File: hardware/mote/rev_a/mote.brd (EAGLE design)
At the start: 160 x 100 mm, 37 parts, among them Q1 CSD22206W, Q2 CSD75207W15, Q3 CSD75207W15, Q4 CSD13303W1015, Q5 CSD22206W, U1 NRF52840, U3 MAX17222, U4 TPS3839G25DBZ, X1 7V-32.000MAHV-T

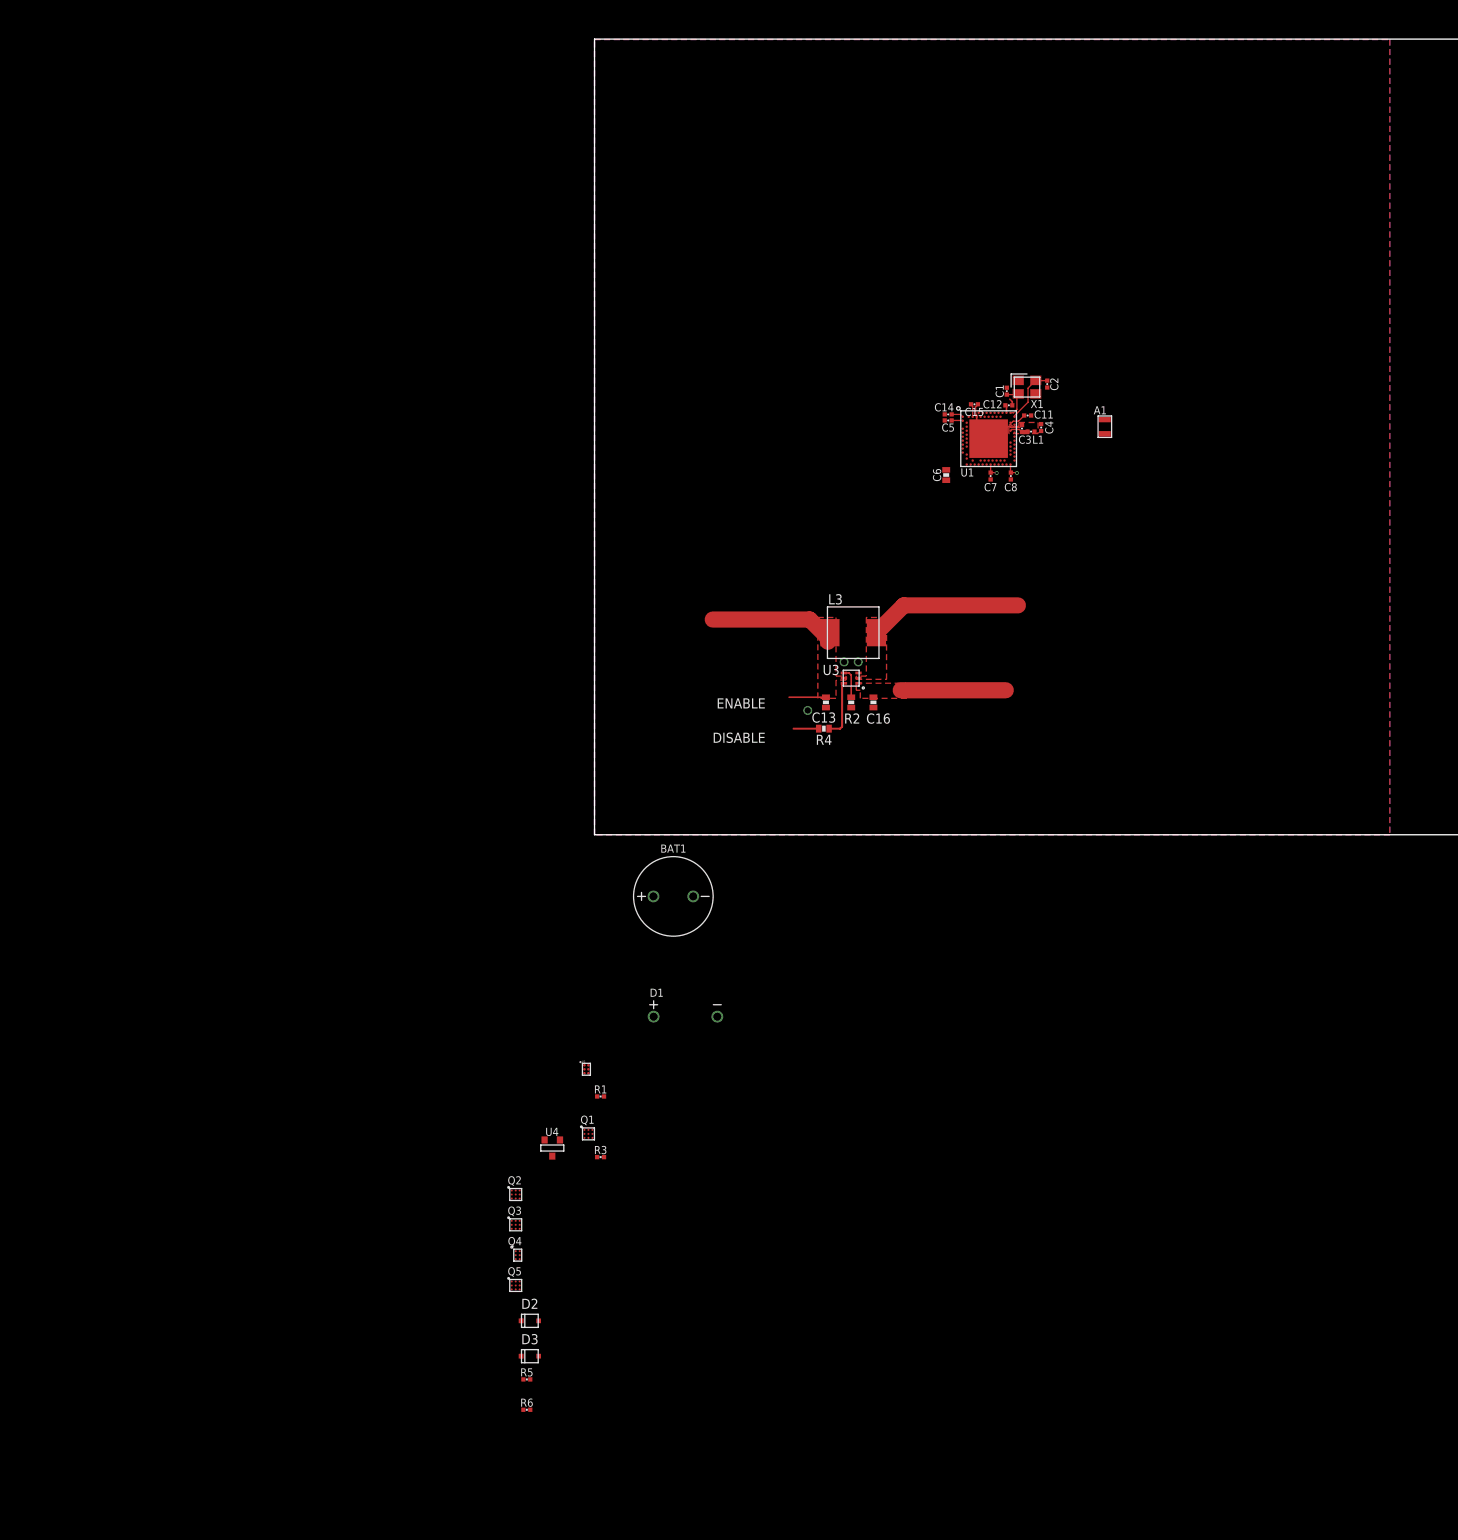
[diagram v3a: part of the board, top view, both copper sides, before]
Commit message: finish power supply, rtc
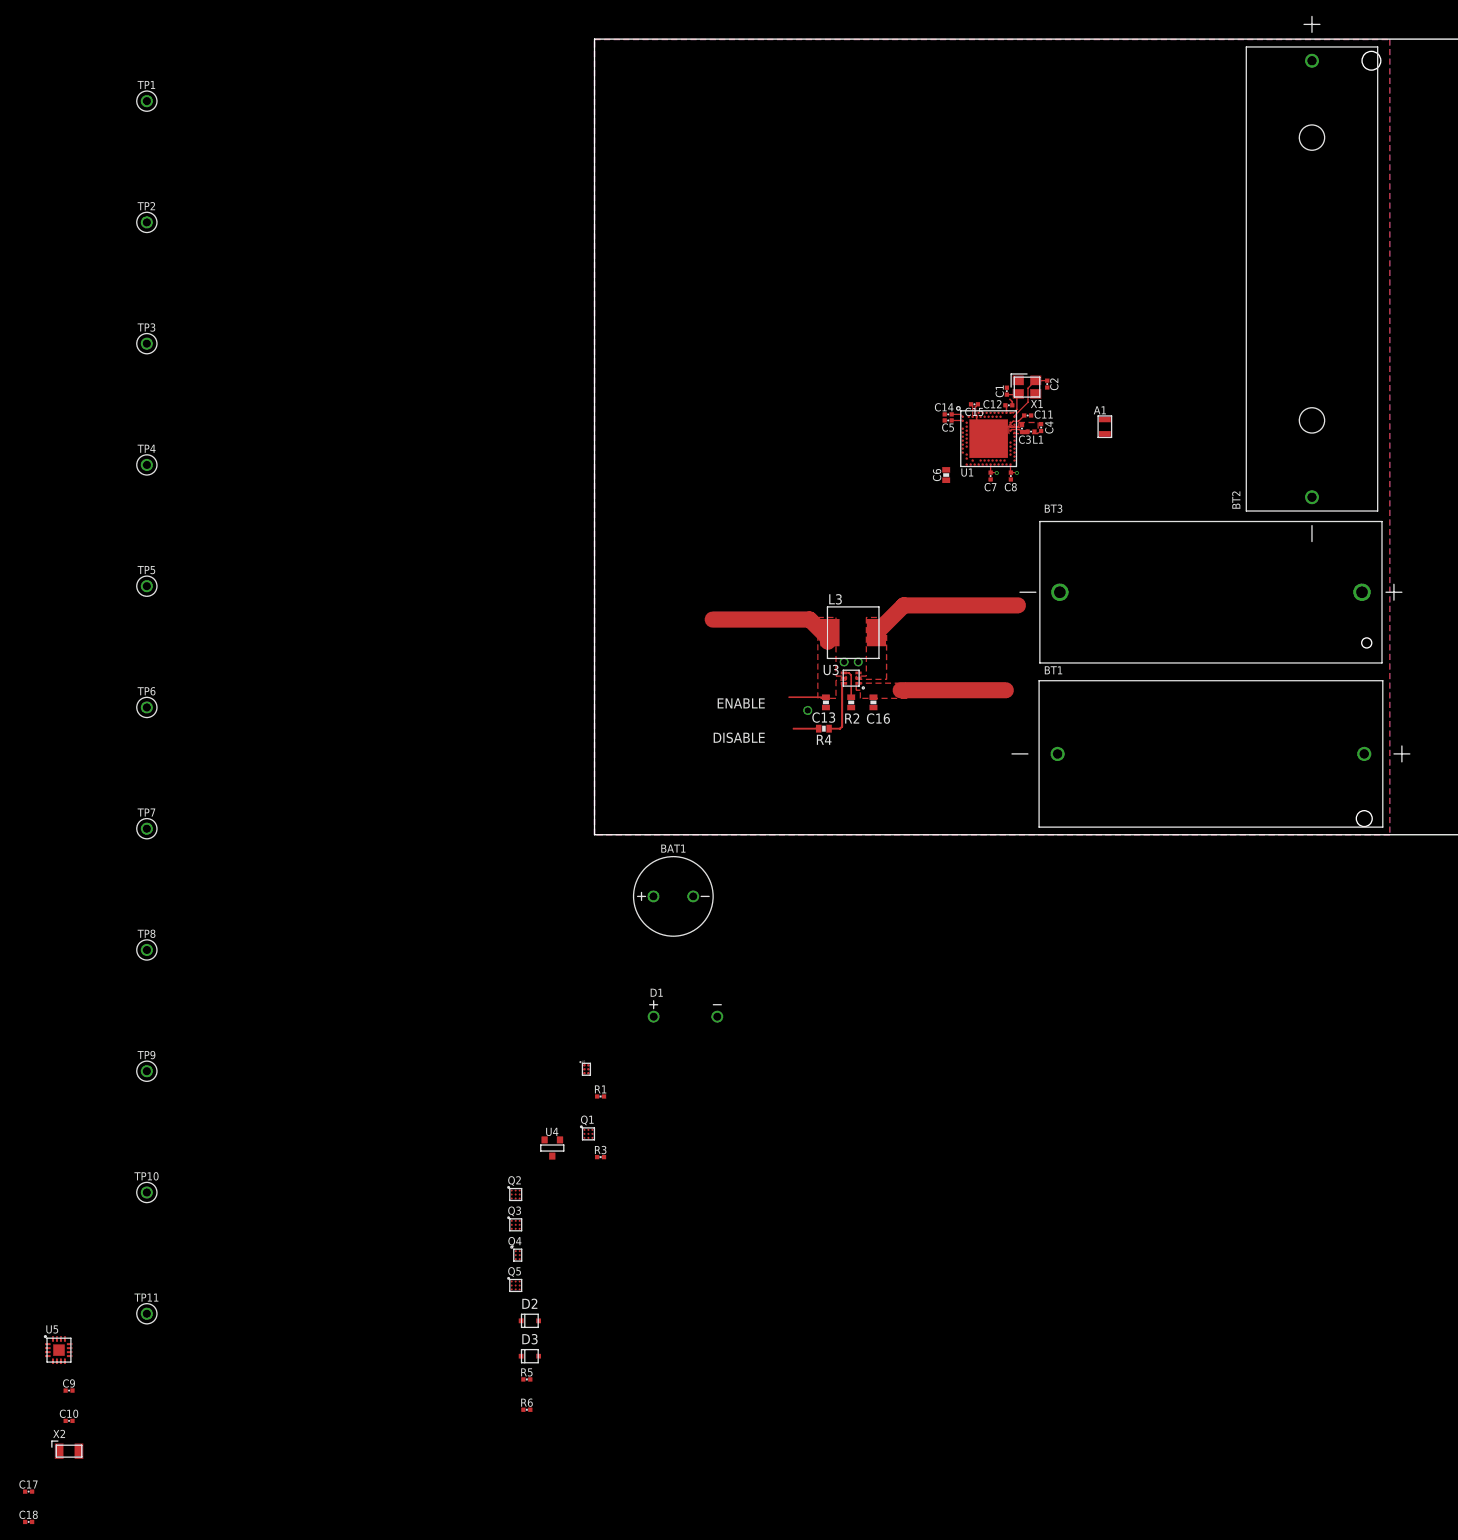
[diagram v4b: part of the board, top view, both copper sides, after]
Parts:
- added BT1: BAT_PACK2/3AA, batteries:6S-2-3A
- added BT2: BAT_PACKAA, batteries:BHAA-3
- added BT3: BAT_PACKCR123A, batteries:BH123A
- added C10: 1uF, passives:0402_CAP
- added C17, C18: DNP, passives:0402_CAP
- added C9: 47pF, passives:0402_CAP
- added TP1, TP10, TP11, TP2, TP3, TP4, TP5, TP6, TP7, TP8, TP9: TEST_POINT_0.040IN, headers:TESTPOINT_0.040IN
- added U5: AB1815-T3, chips:QFN-16-3MM
- added X2: ABS07-32.768KHZ-7-T, crystals:2-SMD
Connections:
- new net !RTC_EXTR: U5.3
- new net !RTC_IRQ1: U5.11
- new net !RTC_IRQ2: U5.4
- new net !RTC_RESET: U5.1
- new net CLKOUT: U1.D2, U5.8
- new net CS_RTC: U5.12
- new net MISO: U5.6
- new net MOSI: U5.9
- new net N$18: D3.P$1, Q3.A1, Q3.C1, R6.2, TP6.TESTPOINT
- new net N$19: C17.1, U5.16, X2.1
- new net N$20: C18.1, U5.15, X2.2
- new net N$21: C9.1, U5.14
- new net N$22: BT1.+, BT2.+, BT3.+, Q3.A2, Q3.A3, Q3.B3, TP9.TESTPOINT
- new net N$24: BAT1.+, D1.+, Q1.C1, Q1.C2, Q1.C3, Q2.A2, Q2.A3, Q2.B3, Q5.C1, Q5.C2, Q5.C3, R1.2, TP1.TESTPOINT, U2.A1, U2.C1, U4.3
- new net SCL: U5.7
- new net WDI: U5.2
- net GND: now also BT1.-, BT2.-, BT3.-, C10.2, C17.2, C18.2, C9.2, U1.F2, U5.GND
- net N$1: now also D2.P$2, Q4.A1, Q4.B1, Q4.C1, Q5.A2, Q5.A3, Q5.B1, Q5.B2, Q5.B3, R5.1, TP4.TESTPOINT; no longer BAT1.+, D1.+, Q1.C1, Q1.C2, Q1.C3, Q5.C1, Q5.C2, Q5.C3, R1.2, U2.A1, U2.C1, U4.3
- net N$10: now also Q2.B1, TP7.TESTPOINT; no longer D2.P$2, Q4.A2, Q5.A1, R5.1, U4.2
- net N$11: now also TP2.TESTPOINT
- net N$13: now also Q2.A1, Q2.C1, TP5.TESTPOINT
- net N$15: now also Q4.A2, Q5.A1, TP3.TESTPOINT, U4.2; no longer Q4.A1, Q4.B1, Q4.C1, Q5.A2, Q5.A3, Q5.B1, Q5.B2, Q5.B3
- net N$16: now also Q3.B1, TP8.TESTPOINT; no longer D3.P$1, R6.2
- net SW1: now also TP11.TESTPOINT
- net VBAT: now also Q2.B2, Q2.C2, Q2.C3, Q3.B2, Q3.C2, Q3.C3, TP10.TESTPOINT
- net VCC: now also C10.1, U5.13

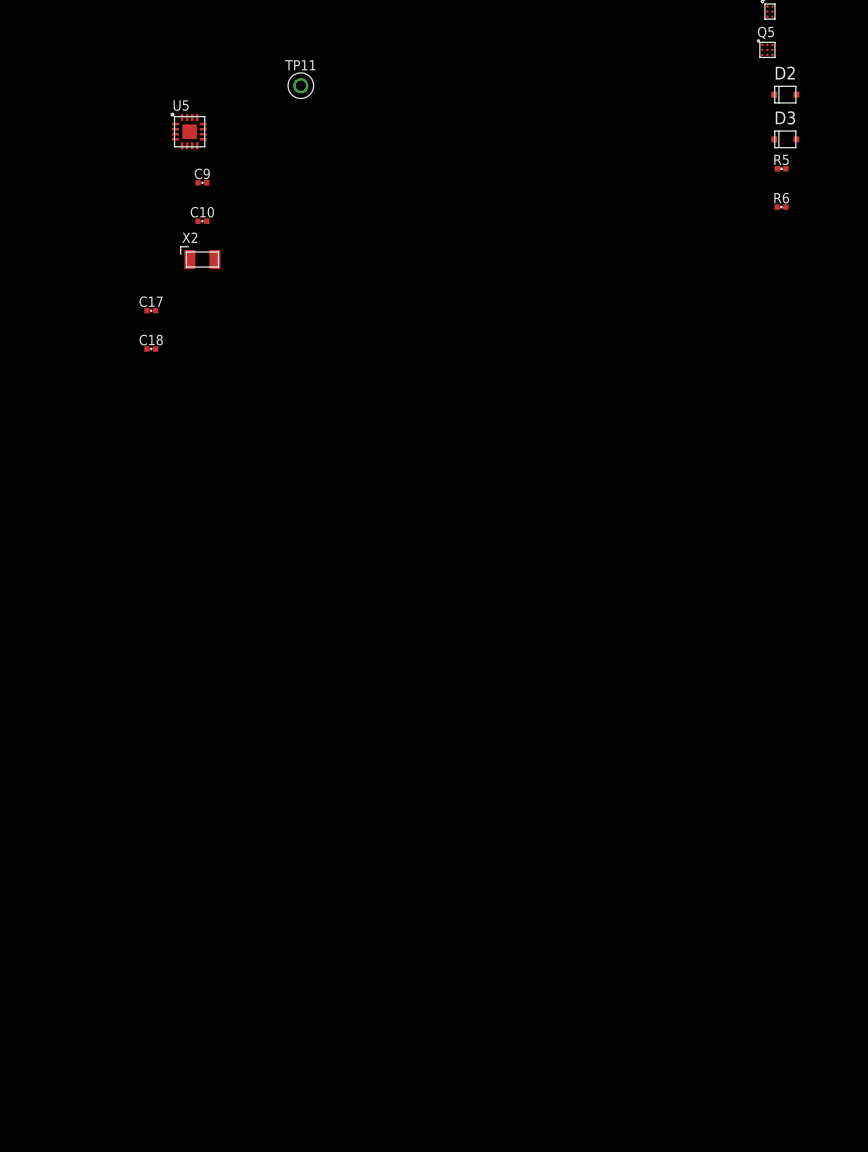
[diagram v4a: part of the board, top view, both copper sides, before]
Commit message: Schematized sensors and cleaned up
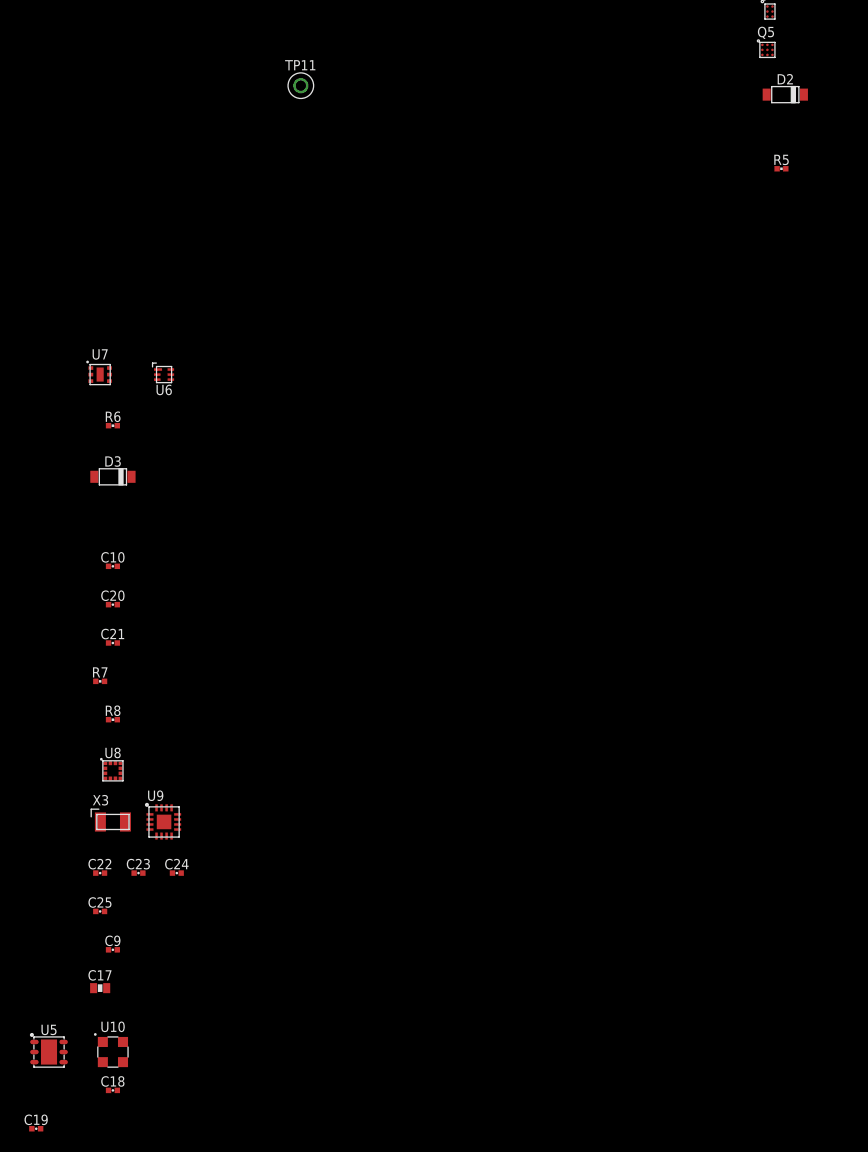
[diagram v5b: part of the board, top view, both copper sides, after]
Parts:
- removed X2: ABS07-32.768KHZ-7-T, crystals:2-SMD
- added C19, C20: 0.1uF, passives:0402_CAP
- added C21, C25: 1.0uF, passives:0402_CAP
- added C22: 47pF, passives:0402_CAP
- added C23, C24: DNP, passives:0402_CAP
- added R7, R8: 10k, passives:0402_RES
- added U10: MS5637-02BA03, chips:4-SMD
- added U6: ISL29125, chips:ODFN-6-1.5MMX1.6MM
- added U7: MAX44009, chips:UDFN-6-EXPOSED
- added U8: LIS2DW12, chips:LGA-12
- added U9: AB1815-T3, chips:QFN-16-3MM
- added X3: ABS07-32.768KHZ-7-T, crystals:2-SMD
- C10: value 1uF -> 1.0uF
- C17: value DNP -> 10uF; device passives:0402_CAP -> passives:0603_CAP
- C18: value DNP -> 0.1uF
- C9: value 47pF -> 0.1uF
- D2, D3: value DIODE_SCHOTTKYSOD323 -> DIODE_SCHOTTKYMBR0520LT1G; device passives:SOD323 -> passives:SOD123
- U5: value AB1815-T3 -> SI7021-A20-GM1; device chips:QFN-16-3MM -> chips:DFN-6/3MM
- moved U5 92.5 mm to (-81.3, -156.2)
- moved C9 76.7 mm to (-74.9, -146.1)
- moved D3 74.7 mm to (-74.9, -99.1)
- moved C18 73.8 mm to (-74.9, -160.0)
- moved R6 69.9 mm to (-74.9, -94.0)
- moved C17 67.5 mm to (-76.2, -149.9)
- moved C10 35.4 mm to (-74.9, -108.0)
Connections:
- removed net N$19: C17.1, U5.16, X2.1
- removed net N$20: C18.1, U5.15, X2.2
- removed net N$21: C9.1, U5.14
- new net !CLR_INT: U6.5
- new net !LGHT_INT: U7.4
- new net ACL_CS: U8.2
- new net ACL_INT1: U8.12
- new net ACL_INT2: U8.11
- new net N$25: C22.1, U9.14
- new net N$26: C23.1, U9.16, X3.1
- new net N$27: C24.1, U9.15, X3.2
- new net SCK: U8.1, U9.7
- new net SDA: R8.1, U10.2, U5.1, U6.4, U7.6
- net !RTC_EXTR: now also U9.3; no longer U5.3
- net !RTC_IRQ1: now also U9.11; no longer U5.11
- net !RTC_IRQ2: now also U9.4; no longer U5.4
- net !RTC_RESET: now also U9.1; no longer U5.1
- net CLKOUT: now also U9.8; no longer U5.8
- net CS_RTC: now also U9.12; no longer U5.12
- net GND: now also C19.2, C20.2, C21.2, C22.2, C23.2, C24.2, C25.2, U10.4, U5.2, U6.3, U7.2, U7.3, U7.EP, U8.5, U8.6, U8.7, U8.8, U9.GND; no longer U5.GND
- net MISO: now also U8.4, U9.6; no longer U5.6
- net MOSI: now also U8.3, U9.9; no longer U5.9
- net N$1: now also D2.A; no longer D2.P$2
- net N$13: now also D2.K; no longer D2.P$1
- net N$15: now also D3.A; no longer D3.P$2
- net N$18: now also D3.K; no longer D3.P$1
- net SCL: now also R7.1, U10.3, U5.6, U6.6, U7.5; no longer U5.7
- net VCC: now also C17.1, C18.1, C19.1, C20.1, C21.1, C25.1, C9.1, R7.2, R8.2, U10.1, U5.5, U6.1, U7.1, U8.10, U8.9, U9.13; no longer U5.13
- net WDI: now also U9.2; no longer U5.2

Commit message: made changes from josh
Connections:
- removed net !RTC_RESET: U9.1
- removed net N$22: BT1.+, BT2.+, BT3.+, Q3.A2, Q3.A3, Q3.B3, TP9.TESTPOINT
- new net !RST: U1.AC13, U9.1
- new net VSW: C13.1, L3.P$1, Q2.B2, Q2.C2, Q2.C3, Q3.B2, Q3.C2, Q3.C3, TP10.TESTPOINT, U3.5
- net N$1: now also Q5.C1, Q5.C2, Q5.C3; no longer Q5.A2, Q5.A3, Q5.B1, Q5.B2, Q5.B3
- net N$24: now also Q5.A2, Q5.A3, Q5.B1, Q5.B2, Q5.B3; no longer Q5.C1, Q5.C2, Q5.C3
- net VBAT: now also BT1.+, BT2.+, BT3.+, C25.1, Q3.A2, Q3.A3, Q3.B3, TP9.TESTPOINT, U9.13; no longer C13.1, L3.P$1, Q2.B2, Q2.C2, Q2.C3, Q3.B2, Q3.C2, Q3.C3, TP10.TESTPOINT, U3.5
- net VCC: no longer C25.1, U9.13
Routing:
- net VSW: track 0.00 -> 4.63 mm
- net VBAT: track 4.63 -> 0.00 mm
